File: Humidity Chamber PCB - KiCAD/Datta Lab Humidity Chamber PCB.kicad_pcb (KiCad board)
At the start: 2 copper layers, 190.5 x 114.3 mm, 49 parts, among them J1 BNC-1, J10 MFC 3, J11 I2C_STANDARDQWIIC, J12 I2C_STANDARDQWIIC, J13 MFC 2, J14 MFC 4, J15 MFM 1, J16 MFM 2, J17 MFC 1, J18 MFC 3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

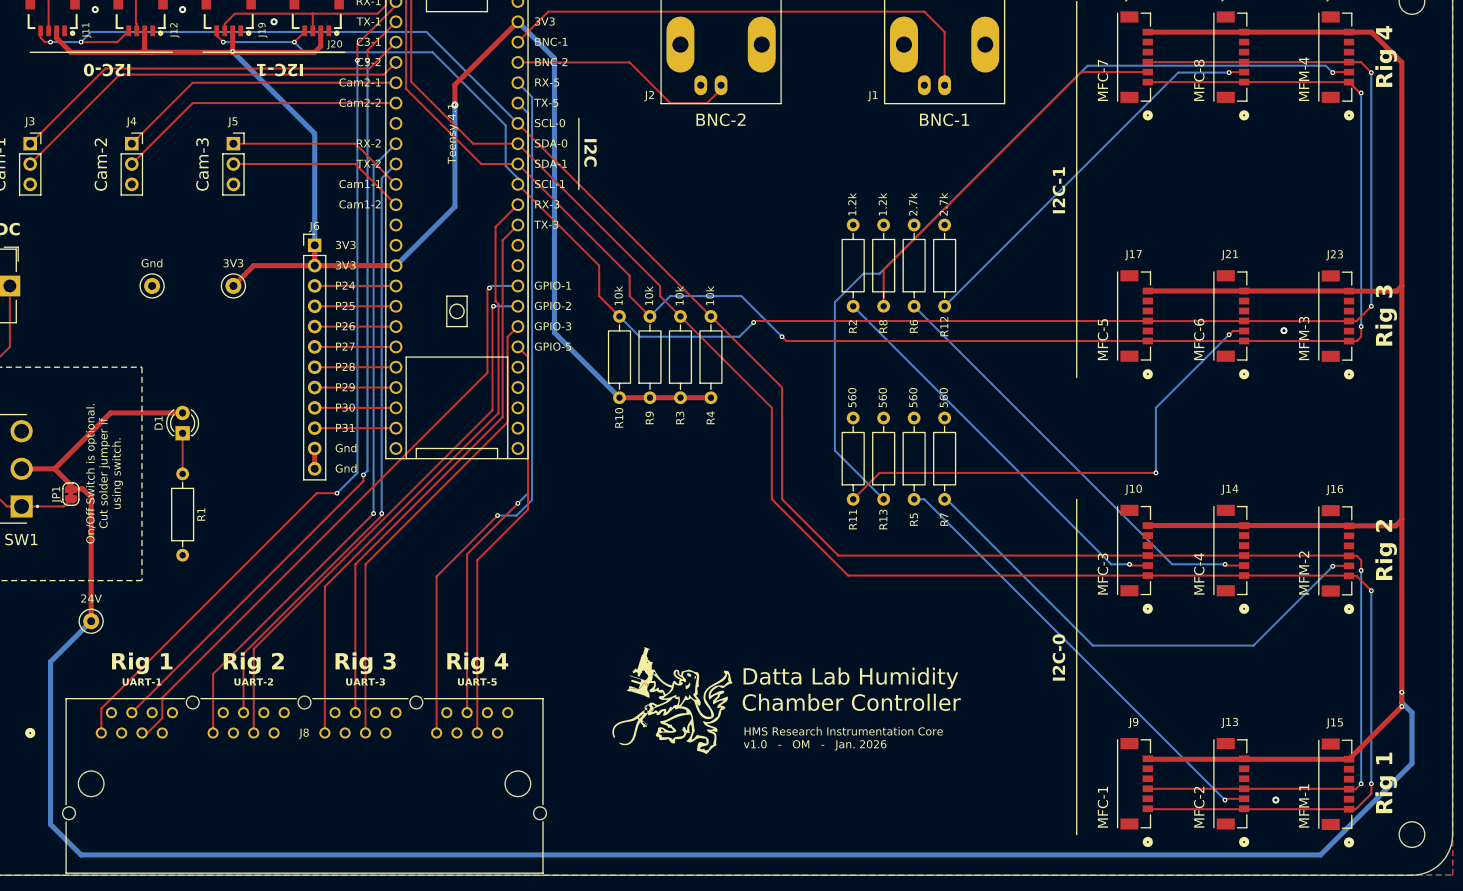
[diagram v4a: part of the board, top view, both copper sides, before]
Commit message: Simplified 24V traces
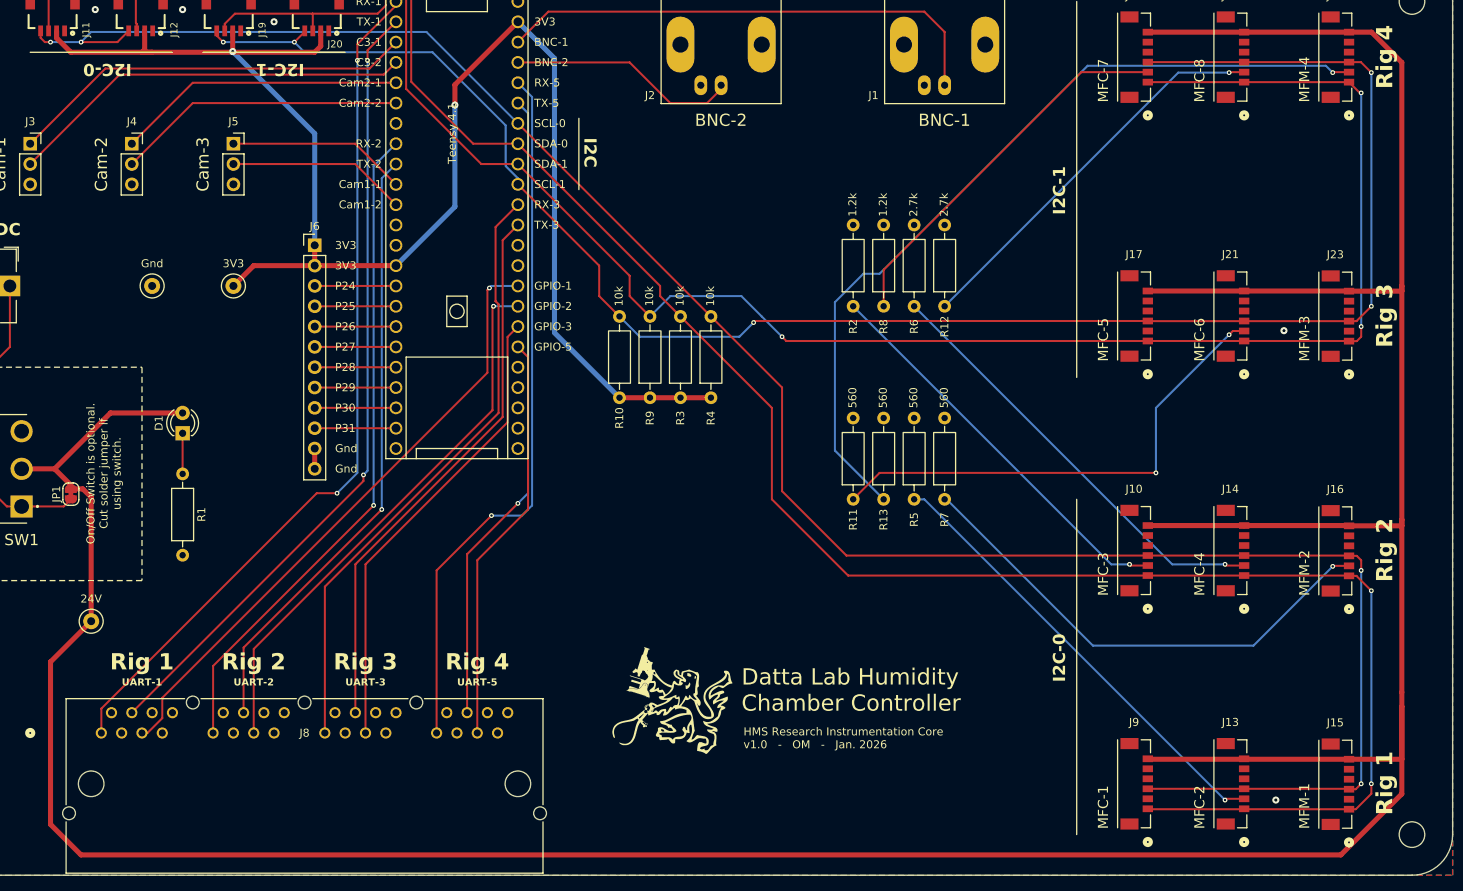
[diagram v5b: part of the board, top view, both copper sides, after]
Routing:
- net +24V: track 471.2 -> 474.1 mm, vias 2 -> 0
- net /RX-5: track 88.4 -> 89.2 mm
- net /SCL-0: track 263.7 -> 263.1 mm

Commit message: Generate Gerbers; A few small tweaks
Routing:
- net /SCL-1: track 227.4 -> 228.7 mm
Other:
- board text added: "C1-1"
- board text added: "C1-2"
- board text added: "Cam3-1"
- board text added: "Cam3-2"
- board text removed: "C3-1"
- board text removed: "C3-2"
- board text removed: "Cam1-1"
- board text removed: "Cam1-2"
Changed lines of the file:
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@@
 			(drillshape 0)
 			(scaleselection 1)
-			(outputdirectory "Gerbers/v4.1/")
+			(outputdirectory "Gerbers/v1.0/")
 		)
 	)
@@
 		)
 	)
-	(gr_text "C3-2"
+	(gr_text "C1-2"
 		(at 92.202 48.26 0)
 		(layer "F.SilkS")
@@
 		)
 	)
-	(gr_text "Cam1-1"
+	(gr_text "Cam3-1"
 		(at 92.202 63.5 0)
 		(layer "F.SilkS")
@@
 		)
 	)
-	(gr_text "Cam1-2"
+	(gr_text "Cam3-2"
 		(at 92.202 66.04 0)
 		(layer "F.SilkS")
@@
 		)
 	)
-	(gr_text "C3-1"
+	(gr_text "C1-1"
 		(at 92.202 45.72 0)
 		(layer "F.SilkS")
@@
 	)
 	(segment
-		(start 119.38 73.66)
-		(end 109.22 63.5)
-		(width 0.254)
-		(layer "F.Cu")
-		(net 10)
-	)
-	(segment
 		(start 82.58048 44.41952)
 		(end 81.28 45.72)
@@
 	)
 	(segment
-		(start 138.875999 80.580001)
-		(end 138.684 80.772)
-		(width 0.254)
-		(layer "F.Cu")
-		(net 10)
-	)
-	(segment
 		(start 215.9 78.74)
 		(end 214.041666 80.598334)
@@
 	)
 	(segment
-		(start 119.38 77.47)
-		(end 119.38 73.66)
+		(start 121.92 80.01)
+		(end 121.92 76.2)
 		(width 0.254)
 		(layer "F.Cu")
@@
 	)
 	(segment
-		(start 121.92 80.01)
-		(end 119.38 77.47)
+		(start 72.39 45.72)
+		(end 71.573813 44.903813)
 		(width 0.254)
 		(layer "F.Cu")
@@
 	)
 	(segment
-		(start 72.39 45.72)
-		(end 71.573813 44.903813)
+		(start 121.92 76.2)
+		(end 109.22 63.5)
 		(width 0.254)
 		(layer "F.Cu")
@@
 	)
 	(segment
-		(start 187.96 80.580001)
-		(end 138.875999 80.580001)
+		(start 142.748 80.580001)
+		(end 187.96 80.580001)
 		(width 0.254)
 		(layer "F.Cu")
@@
 	)
 	(via
-		(at 138.684 80.772)
+		(at 142.748 80.580001)
 		(size 0.6)
 		(drill 0.3)
@@
 	)
 	(segment
-		(start 124.46 82.55)
-		(end 136.906 82.55)
+		(start 138.621999 76.454)
+		(end 125.476 76.454)
 		(width 0.254)
 		(layer "B.Cu")
@@
 	)
 	(segment
-		(start 136.906 82.55)
-		(end 138.684 80.772)
+		(start 142.748 80.580001)
+		(end 138.621999 76.454)
+		(width 0.254)
+		(layer "B.Cu")
+		(net 10)
+	)
+	(segment
+		(start 125.476 76.454)
+		(end 121.92 80.01)
 		(width 0.254)
 		(layer "B.Cu")
@@
 	)
 	(segment
-		(start 121.92 80.01)
-		(end 124.46 82.55)
-		(width 0.254)
-		(layer "B.Cu")
-		(net 10)
-	)
-	(segment
 		(start 109.22 62.738)
 		(end 109.22 63.5)
@@
 	)
 	(segment
-		(start 214.081666 83.098334)
-		(end 214.63 82.55)
-		(width 0.254)
-		(layer "F.Cu")
-		(net 12)
-	)
-	(segment
 		(start 83.58124 44.31284)
 		(end 83.58124 42.17924)
@@
 	)
 	(segment
-		(start 213.114999 83.098334)
-		(end 214.081666 83.098334)
-		(width 0.254)
-		(layer "F.Cu")
-		(net 12)
-	)
-	(segment
 		(start 95.25 39.878)
 		(end 94.742 39.37)
@@
 	)
 	(segment
-		(start 142.24 82.55)
-		(end 142.770001 83.080001)
+		(start 214.081666 83.098334)
+		(end 213.114999 83.098334)
+		(width 0.254)
+		(layer "F.Cu")
+		(net 12)
+	)
+	(segment
+		(start 142.770001 83.080001)
+		(end 187.96 83.080001)
 		(width 0.254)
 		(layer "F.Cu")
@@
 	)
 	(segment
-		(start 109.22 60.96)
-		(end 123.19 74.93)
+		(start 214.63 82.55)
+		(end 214.081666 83.098334)
 		(width 0.254)
 		(layer "F.Cu")
@@
 	)
 	(segment
-		(start 125.73 80.01)
-		(end 123.19 77.47)
+		(start 109.22 60.96)
+		(end 125.73 77.47)
 		(width 0.254)
 		(layer "F.Cu")
@@
 	)
 	(segment
-		(start 123.19 74.93)
-		(end 123.19 77.47)
-		(width 0.254)
-		(layer "F.Cu")
-		(net 12)
-	)
-	(segment
 		(start 95.25 51.562)
 		(end 95.25 39.878)
@@
 	)
 	(segment
-		(start 214.63 82.55)
-		(end 214.63 81.28)
+		(start 125.73 77.47)
+		(end 125.73 80.01)
 		(width 0.254)
 		(layer "F.Cu")
@@
 		(net 12)
 	)
-	(segment
-		(start 142.770001 83.080001)
-		(end 187.96 83.080001)
-		(width 0.254)
-		(layer "F.Cu")
-		(net 12)
-	)
 	(via
 		(at 214.63 52.07)
@@
 	)
 	(via
-		(at 142.24 82.55)
+		(at 142.770001 83.080001)
 		(size 0.6)
 		(drill 0.3)
@@
 	)
 	(via
-		(at 214.63 81.28)
+		(at 214.63 82.55)
 		(size 0.6)
 		(drill 0.3)
@@
 	)
 	(segment
-		(start 137.16 77.47)
-		(end 128.27 77.47)
-		(width 0.254)
-		(layer "B.Cu")
-		(net 12)
-	)
-	(segment
-		(start 139.7 80.01)
+		(start 142.770001 83.080001)
 		(end 137.16 77.47)
 		(width 0.254)
@@
 	)
 	(segment
-		(start 139.7 80.01)
-		(end 142.24 82.55)
+		(start 137.16 77.47)
+		(end 128.27 77.47)
 		(width 0.254)
 		(layer "B.Cu")
@@
 	)
 	(segment
-		(start 214.63 81.28)
+		(start 214.63 82.55)
 		(end 214.63 52.07)
 		(width 0.254)
@@
 	)
 	(segment
-		(start 57.15 132.08)
-		(end 57.15 129.032)
-		(width 0.254)
-		(layer "F.Cu")
-		(net 40)
-	)
-	(segment
-		(start 84.074 102.108)
-		(end 86.614 102.108)
+		(start 57.15 129.032)
+		(end 57.15 132.08)
 		(width 0.254)
 		(layer "F.Cu")
@@
 	)
 	(segment
-		(start 93.98 41.148)
-		(end 93.98 40.64)
+		(start 84.074 102.108)
+		(end 57.15 129.032)
 		(width 0.254)
 		(layer "F.Cu")
@@
 	)
 	(segment
-		(start 57.15 129.032)
-		(end 84.074 102.108)
+		(start 93.98 41.148)
+		(end 93.98 40.64)
 		(width 0.254)
 		(layer "F.Cu")
@@
 	)
 	(via
-		(at 86.614 102.108)
+		(at 84.074 102.108)
 		(size 0.6)
 		(drill 0.3)
@@
 	)
 	(segment
+		(start 84.074 102.108)
+		(end 86.614 102.108)
+		(width 0.254)
+		(layer "B.Cu")
+		(net 40)
+	)
+	(segment
 		(start 89.154 99.568)
 		(end 89.154 48.006)
@@
 	)
 	(segment
-		(start 150.499999 112.399999)
-		(end 140.97 102.87)
-		(width 0.254)
-		(layer "F.Cu")
-		(net 55)
-	)
-	(segment
 		(start 95.885 37.803)
 		(end 94.912 36.83)
@@
 	)
 	(segment
+		(start 187.96 112.399999)
+		(end 150.499999 112.399999)
+		(width 0.254)
+		(layer "F.Cu")
+		(net 55)
+	)
+	(segment
 		(start 188.014999 141.609999)
 		(end 187.96 141.555)
@@
 	)
 	(segment
-		(start 187.96 112.399999)
-		(end 150.499999 112.399999)
+		(start 129.54 78.74)
+		(end 109.22 58.42)
 		(width 0.254)
 		(layer "F.Cu")
@@
 	)
 	(segment
-		(start 140.97 91.44)
-		(end 127 77.47)
+		(start 129.54 80.01)
+		(end 129.54 78.74)
+		(width 0.254)
+		(layer "F.Cu")
+		(net 55)
+	)
+	(segment
+		(start 140.97 102.87)
+		(end 140.97 91.44)
 		(width 0.254)
 		(layer "F.Cu")
@@
 	)
 	(segment
-		(start 127 77.47)
-		(end 127 76.2)
+		(start 140.97 91.44)
+		(end 129.54 80.01)
 		(width 0.254)
 		(layer "F.Cu")
@@
 	)
 	(segment
-		(start 140.97 102.87)
-		(end 140.97 91.44)
+		(start 150.499999 112.399999)
+		(end 140.97 102.87)
 		(width 0.254)
 		(layer "F.Cu")
@@
 	)
 	(segment
-		(start 127 76.2)
-		(end 109.22 58.42)
-		(width 0.254)
-		(layer "F.Cu")
-		(net 55)
-	)
-	(segment
 		(start 215.9 139.672698)
 		(end 213.962699 141.609999)
@@
 		(hatch edge 0.5)
 		(connect_pads
-			(clearance 0.5)
+			(clearance 0.4064)
 		)
-		(min_thickness 0.25)
+		(min_thickness 0.2032)
 		(filled_areas_thickness no)
 		(fill yes

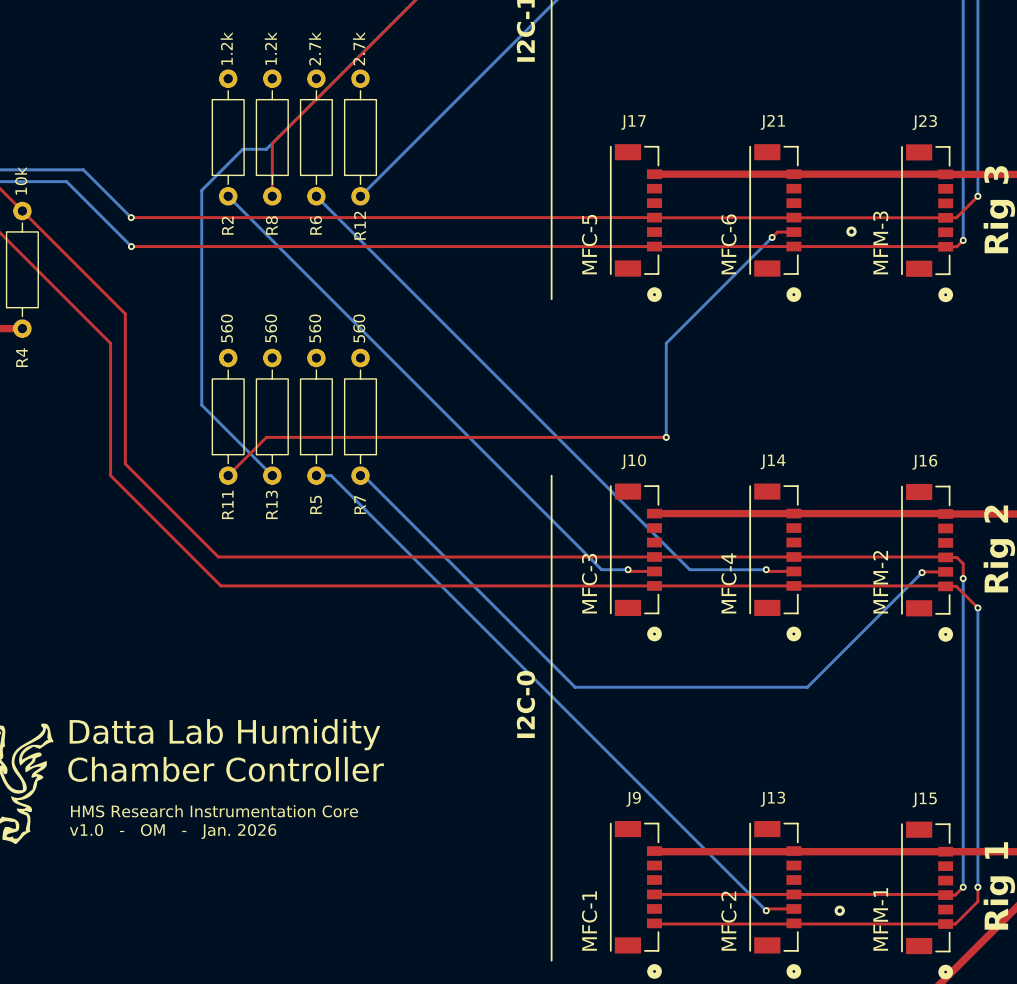
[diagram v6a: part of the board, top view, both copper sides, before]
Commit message: Start v1.1.   Fix address resistors for MFMs
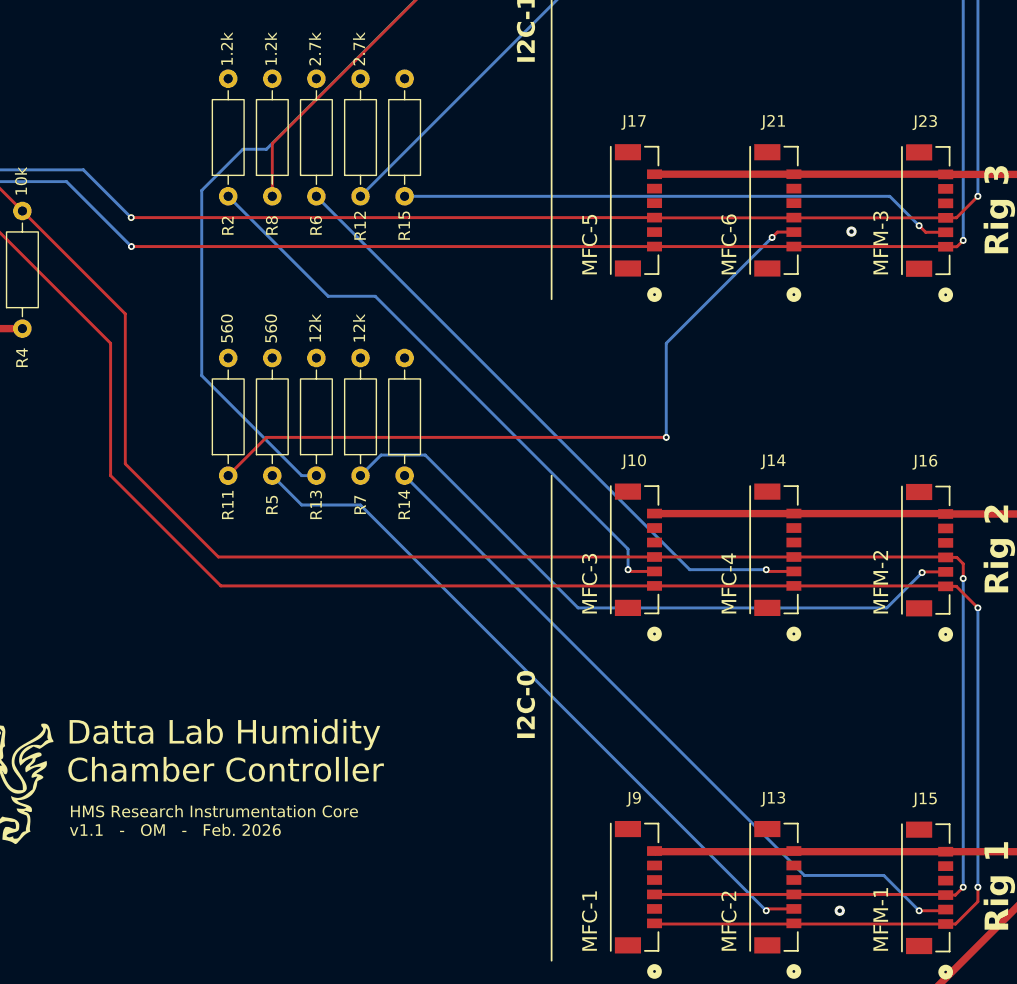
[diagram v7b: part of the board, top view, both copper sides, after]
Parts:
- added R14: 5.6k, Resistor_THT:R_Axial_DIN0207_L6.3mm_D2.5mm_P10.16mm_Horizontal, F.Cu at (166.4, 102.9)
- added R15: 5.6k, Resistor_THT:R_Axial_DIN0207_L6.3mm_D2.5mm_P10.16mm_Horizontal, F.Cu at (166.4, 78.7)
- R13, R7: value 560 -> 12k
- moved R13 3.81 mm to (158.8, 102.9)
- moved R5 3.81 mm to (154.9, 102.9)
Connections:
- J15 pad 2: GND -> Net-(J15-Pin_2)
- J23 pad 2: GND -> Net-(J23-Pin_2)
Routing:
- net Net-(J15-Pin_2): track 0.00 -> 62.4 mm, vias 0 -> 1
- net Net-(J23-Pin_2): track 0.00 -> 48.0 mm, vias 0 -> 1
- net Net-(J16-Pin_2): track 62.3 -> 58.3 mm
- net Net-(J13-Pin_2): track 56.9 -> 60.7 mm
- net Net-(J24-Pin_2): track 104.1 -> 106.4 mm
- net Net-(J10-Pin_2): track 50.3 -> 51.3 mm
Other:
- board text added: "HMS Research Instrumentation Core v1.1 - OM - Feb. 2026"
- board text removed: "HMS Research Instrumentation Core v1.0 - OM - Jan. 2026"
